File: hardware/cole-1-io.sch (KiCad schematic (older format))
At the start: 12 parts, among them J1 Port A, J2 Port B, J3 TTL Serial, U10 MC68B50, U6 74HCT04, U9 WD65C22, Y1 1.8432 MHz

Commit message: - Change WE on the EEPROM to be tied to ground, like it is on the breadboard prototype. - Change TD pin on the MAX1232 to bre tied to Vcc, which raises the watchdog timeout to 1.2s. - Add Vcc and GND pins to each of the GPIO headers
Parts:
- D1: value D_Schottky_Small -> BA85
- J1, J2: footprint Pin_Headers:Pin_Header_Straight_1x10_Pitch2.54mm -> Pin_Headers:Pin_Header_Straight_1x12_Pitch2.54mm; symbol Conn_01x10 -> Conn_01x12
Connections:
- wire segments 118 -> 126

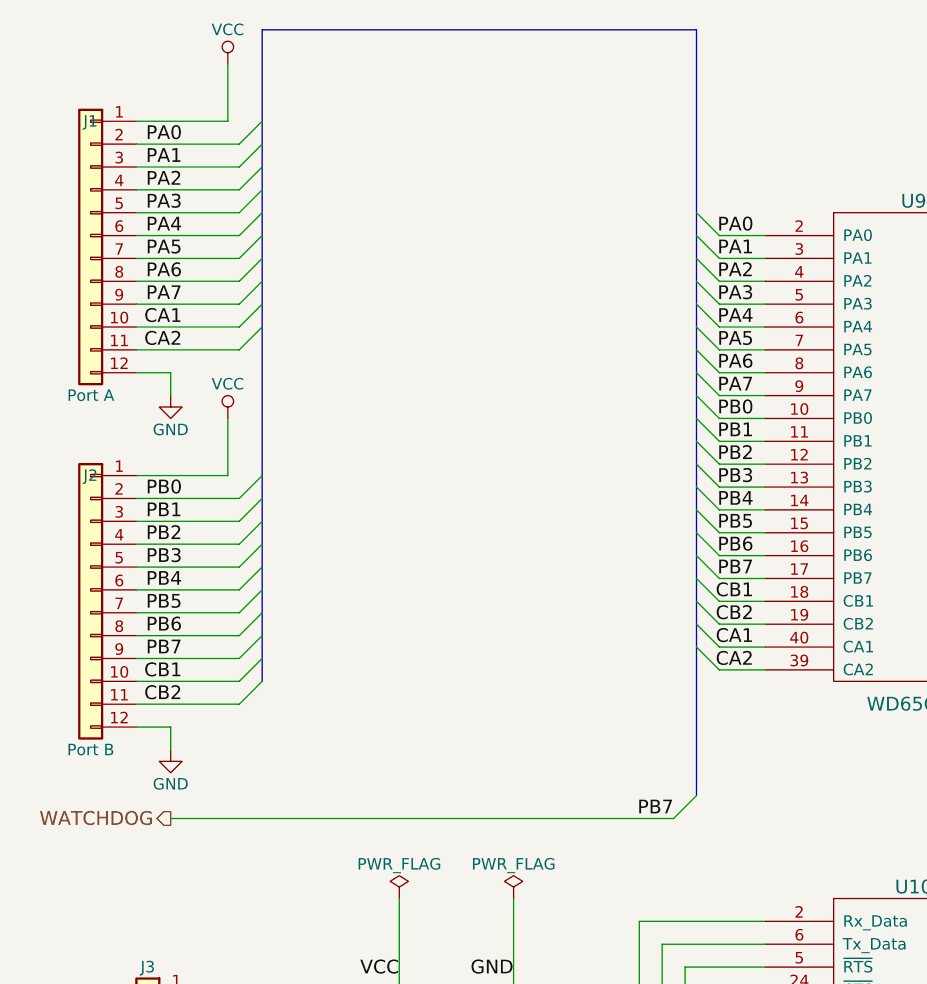
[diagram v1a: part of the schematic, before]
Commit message: change VIA port connectors to 2x12 connectors with per-signal ground wires
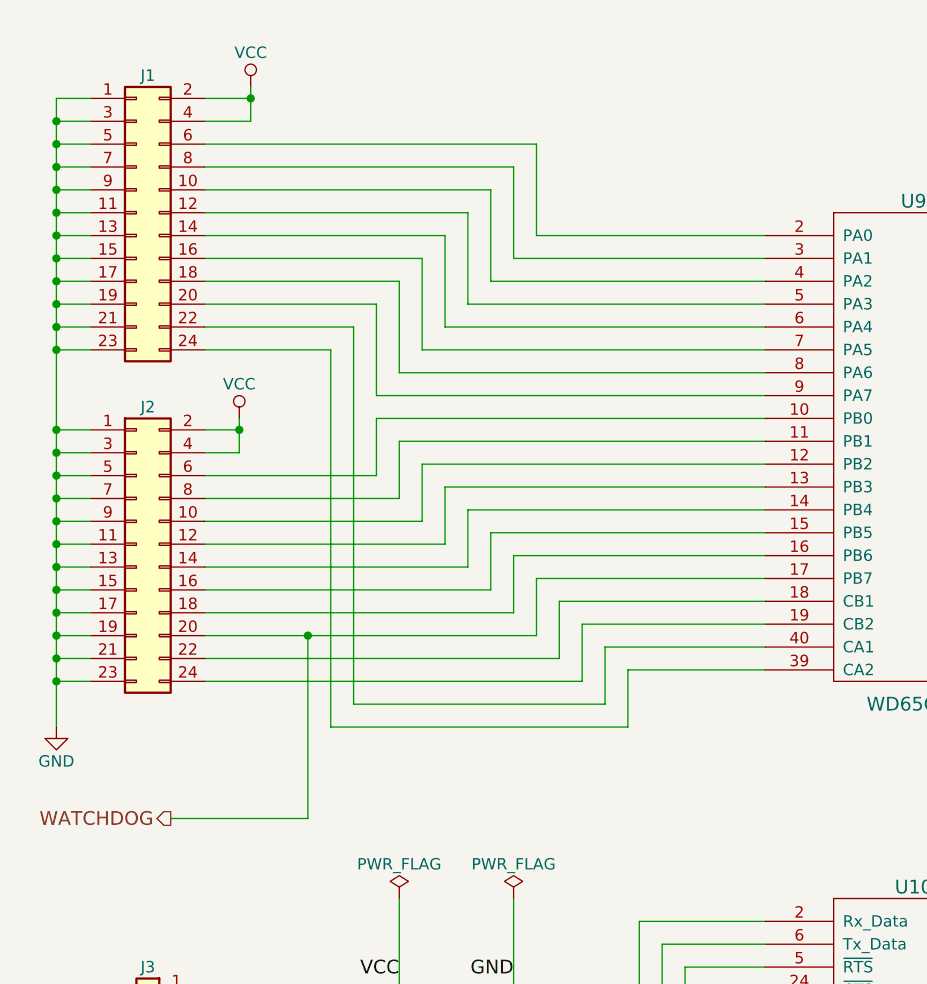
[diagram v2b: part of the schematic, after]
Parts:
- removed J1: Port A, Pin_Headers:Pin_Header_Straight_1x12_Pitch2.54mm, symbol Conn_01x12
- removed J2: Port B, Pin_Headers:Pin_Header_Straight_1x12_Pitch2.54mm, symbol Conn_01x12
- added J1, J2: Conn_02x12_Odd_Even, symbol Conn_02x12_Odd_Even
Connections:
- net GND: now also J1.1 (Pin_1), J1.11 (Pin_11), J1.13 (Pin_13), J1.15 (Pin_15), J1.17 (Pin_17), J1.19 (Pin_19), J1.21 (Pin_21), J1.23 (Pin_23), J1.3 (Pin_3), J1.5 (Pin_5), J1.7 (Pin_7), J1.9 (Pin_9), J2.1 (Pin_1), J2.11 (Pin_11), J2.13 (Pin_13), J2.15 (Pin_15), J2.17 (Pin_17), J2.19 (Pin_19), J2.21 (Pin_21), J2.23 (Pin_23), J2.3 (Pin_3), J2.5 (Pin_5), J2.7 (Pin_7), J2.9 (Pin_9)
- net VCC: now also J1.2 (Pin_2), J1.4 (Pin_4), J2.2 (Pin_2), J2.4 (Pin_4)
- net WATCHDOG: now also J2.20 (Pin_20)
- net CA1: no longer names the net of U9.40 (CA1)
- net CA1: now also J1.22 (Pin_22)
- net CA2: no longer names the net of U9.39 (CA2)
- net CA2: now also J1.24 (Pin_24)
- net CB1: no longer names the net of U9.18 (CB1)
- net CB1: now also J2.22 (Pin_22)
- net CB2: no longer names the net of U9.19 (CB2)
- net CB2: now also J2.24 (Pin_24)
- net PA0: no longer names the net of U9.2 (PA0)
- net PA0: now also J1.6 (Pin_6)
- net PA1: no longer names the net of U9.3 (PA1)
- net PA1: now also J1.8 (Pin_8)
- net PA2: no longer names the net of U9.4 (PA2)
- net PA2: now also J1.10 (Pin_10)
- net PA3: no longer names the net of U9.5 (PA3)
- net PA3: now also J1.12 (Pin_12)
- net PA4: no longer names the net of U9.6 (PA4)
- net PA4: now also J1.14 (Pin_14)
- net PA5: no longer names the net of U9.7 (PA5)
- net PA5: now also J1.16 (Pin_16)
- net PA6: no longer names the net of U9.8 (PA6)
- net PA6: now also J1.18 (Pin_18)
- net PA7: no longer names the net of U9.9 (PA7)
- net PA7: now also J1.20 (Pin_20)
- net PB0: no longer names the net of U9.10 (PB0)
- net PB0: now also J2.6 (Pin_6)
- net PB1: no longer names the net of U9.11 (PB1)
- net PB1: now also J2.8 (Pin_8)
- net PB2: no longer names the net of U9.12 (PB2)
- net PB2: now also J2.10 (Pin_10)
- net PB3: no longer names the net of U9.13 (PB3)
- net PB3: now also J2.12 (Pin_12)
- net PB4: no longer names the net of U9.14 (PB4)
- net PB4: now also J2.14 (Pin_14)
- net PB5: no longer names the net of U9.15 (PB5)
- net PB5: now also J2.16 (Pin_16)
- net PB6: no longer names the net of U9.16 (PB6)
- net PB6: now also J2.18 (Pin_18)

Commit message: Final schematic and PCB layout.
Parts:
- C12: renamed from C2; footprint Capacitors_THT:C_Disc_D4.7mm_W2.5mm_P5.00mm -> Capacitors_SMD:C_0805_HandSoldering
- J1: value Conn_02x12_Odd_Even -> PORT A; footprint (none) -> Pin_Headers:Pin_Header_Straight_1x12_Pitch2.54mm; symbol Conn_02x12_Odd_Even -> Conn_01x12
- J2: value Conn_02x12_Odd_Even -> PORT B; footprint (none) -> Pin_Headers:Pin_Header_Straight_1x12_Pitch2.54mm; symbol Conn_02x12_Odd_Even -> Conn_01x12
- R7, R8, R9: footprint Resistors_THT:R_Axial_DIN0207_L6.3mm_D2.5mm_P10.16mm_Horizontal -> Resistors_SMD:R_0805_HandSoldering
- U10: footprint Housings_DIP:DIP-24_W10.16mm_Socket_LongPads -> Housings_DIP:DIP-24_W10.16mm_Socket
- U6: footprint Housings_DIP:DIP-14_W7.62mm_Socket_LongPads -> Housings_DIP:DIP-14_W7.62mm_Socket
- U9: footprint Housings_DIP:DIP-40_W15.24mm_Socket_LongPads -> Housings_DIP:DIP-40_W15.24mm_Socket
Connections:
- net GND: now also J1.12 (Pin_12), J2.12 (Pin_12); no longer J1.1 (Pin_1), J1.11 (Pin_11), J1.13 (Pin_13), J1.15 (Pin_15), J1.17 (Pin_17), J1.19 (Pin_19), J1.21 (Pin_21), J1.23 (Pin_23), J1.3 (Pin_3), J1.5 (Pin_5), J1.7 (Pin_7), J1.9 (Pin_9), J2.1 (Pin_1), J2.11 (Pin_11), J2.13 (Pin_13), J2.15 (Pin_15), J2.17 (Pin_17), J2.19 (Pin_19), J2.21 (Pin_21), J2.23 (Pin_23), J2.3 (Pin_3), J2.5 (Pin_5), J2.7 (Pin_7), J2.9 (Pin_9)
- net VCC: now also J1.1 (Pin_1), J2.1 (Pin_1); no longer J1.2 (Pin_2), J1.4 (Pin_4), J2.2 (Pin_2), J2.4 (Pin_4)
- net at U9.10 (PB0): now also J2.2 (Pin_2); no longer J2.6 (Pin_6)
- net at U9.11 (PB1): now also J2.3 (Pin_3); no longer J2.8 (Pin_8)
- net at U9.12 (PB2): now also J2.4 (Pin_4); no longer J2.10 (Pin_10)
- net at U9.13 (PB3): now also J2.5 (Pin_5); no longer J2.12 (Pin_12)
- net at U9.14 (PB4): now also J2.6 (Pin_6); no longer J2.14 (Pin_14)
- net at U9.15 (PB5): now also J2.7 (Pin_7); no longer J2.16 (Pin_16)
- net at U9.16 (PB6): now also J2.8 (Pin_8); no longer J2.18 (Pin_18)
- net at U9.18 (CB1): now also J2.10 (Pin_10); no longer J2.22 (Pin_22)
- net at U9.19 (CB2): now also J2.11 (Pin_11); no longer J2.24 (Pin_24)
- net at U9.2 (PA0): now also J1.2 (Pin_2); no longer J1.6 (Pin_6)
- net at U9.3 (PA1): now also J1.3 (Pin_3); no longer J1.8 (Pin_8)
- net at U9.39 (CA2): now also J1.11 (Pin_11); no longer J1.24 (Pin_24)
- net at U9.4 (PA2): now also J1.4 (Pin_4); no longer J1.10 (Pin_10)
- net at U9.40 (CA1): now also J1.10 (Pin_10); no longer J1.22 (Pin_22)
- net at U9.5 (PA3): now also J1.5 (Pin_5); no longer J1.12 (Pin_12)
- net at U9.6 (PA4): now also J1.6 (Pin_6); no longer J1.14 (Pin_14)
- net at U9.7 (PA5): now also J1.7 (Pin_7); no longer J1.16 (Pin_16)
- net at U9.8 (PA6): now also J1.8 (Pin_8); no longer J1.18 (Pin_18)
- net at U9.9 (PA7): now also J1.9 (Pin_9); no longer J1.20 (Pin_20)
- net WATCHDOG: no longer names the net of U9.17 (PB7)
- net WATCHDOG: now also J2.9 (Pin_9); no longer J2.20 (Pin_20)

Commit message: fix footprint for the ACIA
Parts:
- U10: footprint Housings_DIP:DIP-24_W10.16mm_Socket -> Housings_DIP:DIP-24_W15.24mm_Socket
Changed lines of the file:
@@
 F 0 "U10" H 4550 6250 60  0000 C CNN
 F 1 "MC68B50" H 4550 4450 60  0000 C CNN
-F 2 "Housings_DIP:DIP-24_W10.16mm_Socket" H 4550 4700 60  0001 C CNN
+F 2 "Housings_DIP:DIP-24_W15.24mm_Socket" H 4550 4700 60  0001 C CNN
 F 3 "" H 4550 4700 60  0000 C CNN
 	1    4550 5350

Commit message: Updated schematics, board layout, and GAL code for COLE-1+
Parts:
- removed C12: 270p, Capacitors_SMD:C_0805_HandSoldering, symbol C_Small
- removed D1: BA85, Diodes_THT:D_A-405_P10.16mm_Horizontal, symbol D_Schottky_Small
- removed J1: PORT A, Pin_Headers:Pin_Header_Straight_1x12_Pitch2.54mm, symbol Conn_01x12
- removed J2: PORT B, Pin_Headers:Pin_Header_Straight_1x12_Pitch2.54mm, symbol Conn_01x12
- removed J3: TTL Serial, Pin_Headers:Pin_Header_Straight_1x06_Pitch2.54mm, symbol Conn_01x06
- removed R7, R8: 2K2, Resistors_SMD:R_0805_HandSoldering, symbol R_Small
- removed R9: 3.3K, Resistors_SMD:R_0805_HandSoldering, symbol R_Small
- removed U10: MC68B50, Housings_DIP:DIP-24_W15.24mm_Socket, symbol MC6850_
- removed U6: 74HCT04, Housings_DIP:DIP-14_W7.62mm_Socket, symbol 74HCT04
- removed U9: WD65C22, Housings_DIP:DIP-40_W15.24mm_Socket, symbol WD65C22
- removed Y1: 1.8432 MHz, Crystals:Crystal_HC49-U_Vertical, symbol Crystal
